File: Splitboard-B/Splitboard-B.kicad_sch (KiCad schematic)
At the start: 109 parts, among them J4 USB_C_Receptacle, K39 KEYSW, K40 KEYSW, K41 KEYSW, K42 KEYSW, K43 KEYSW, K44 KEYSW, K45 KEYSW, K46 KEYSW, K47 KEYSW, K48 KEYSW, K49 KEYSW, K50 KEYSW, K51 KEYSW, K52 KEYSW, K53 KEYSW, K54 KEYSW, K55 KEYSW, K56 KEYSW, K57 KEYSW, K58 KEYSW, K59 KEYSW, K60 KEYSW, K61 KEYSW, K62 KEYSW, K63 KEYSW, K64 KEYSW, K65 KEYSW, K66 KEYSW, K67 KEYSW, K68 KEYSW, K69 KEYSW, K70 KEYSW, K71 KEYSW, K72 KEYSW, K73 KEYSW, K74 KEYSW, K75 KEYSW, K76 KEYSW, U5 CR2013-MI2120

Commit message: updated USB, LCD, ESD, Voltage Reg in schematic
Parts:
- removed C17, C18, C19, C20, C21, C22, C23, C24: 100nF, symbol Device:C
- removed F?: 500mA, Fuse:Fuse_BelFuse_0ZRE0125FF_L21.2mm_W5.3mm, symbol Device:Fuse
- removed R6, R8: 4.7K, symbol Device:R
- added R? (x2): 4K7, symbol Device:R
- added R?: 10k, Resistor_SMD:R_0805_2012Metric, symbol Device:R
- J4: footprint USB_C_Receptacle_GCT_USB4085 -> Connector_USB:USB_C_Receptacle_Amphenol_12401548E4-2A
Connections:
- net +3.3V: now also U5.8 (LED), R?.1, R?.1, R?.2
- net ENC_A: now also U?.1 (GPB0); no longer U?.27 (GPA6)
- net ENC_B: now also U?.2 (GPB1); no longer U?.28 (GPA7)
- net ENC_SW: now also U?.27 (GPA6), R?.1; no longer U?.1 (GPB0)
- net MOSI: now also J4.A5 (CC1), J4.B5 (CC2); no longer J4.B11 (RX1+)
- net SCK: now also J4.A8 (SBU1), J4.B8 (SBU2); no longer J4.A2 (TX1+)
- net SCL: now also J4.A7 (D-), J4.B7 (D-), R?.2; no longer J4.A10 (RX2-)
- net SDA: now also J4.A6 (D+), J4.B6 (D+), R?.2; no longer J4.A11 (RX2+)
- net row0: now also U?.3 (GPB2); no longer U?.2 (GPB1)
- net row1: now also U?.4 (GPB3); no longer U?.3 (GPB2)
- net row2: now also U?.5 (GPB4); no longer U?.4 (GPB3)
- net row3: now also U?.6 (GPB5); no longer U?.5 (GPB4)
- net row4: now also U?.7 (GPB6); no longer U?.6 (GPB5)
- net row5: now also U?.8 (GPB7); no longer U?.7 (GPB6)
- net row6: now also U?.28 (GPA7); no longer U?.8 (GPB7)
- net LCD2_RST: now reaches J4.B3 (TX2-)
- net LCD2_RST: now also J4.A3 (TX1-)
- net LCD2_RESET: now reaches U5.4 (RESET)
- net LCD2_DC: now reaches U5.5 (D/~{C})
- net LCD2_DC: now also J4.A11 (RX2+), J4.B11 (RX1+)
- net at D?.1 (K): now also FB?.1
- net CS renamed LCD2_CS
- net LCD2_CS: now also J4.A10 (RX2-)
- net MISO: no longer names the net of U5.9 (MISO)
- net MISO: no longer J4.A3 (TX1-)
- no-connect marks 6 -> 9
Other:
- note removed: "I2C Pullup"
- moved on the sheet: C15, C16, C?, D?, FB?, U?

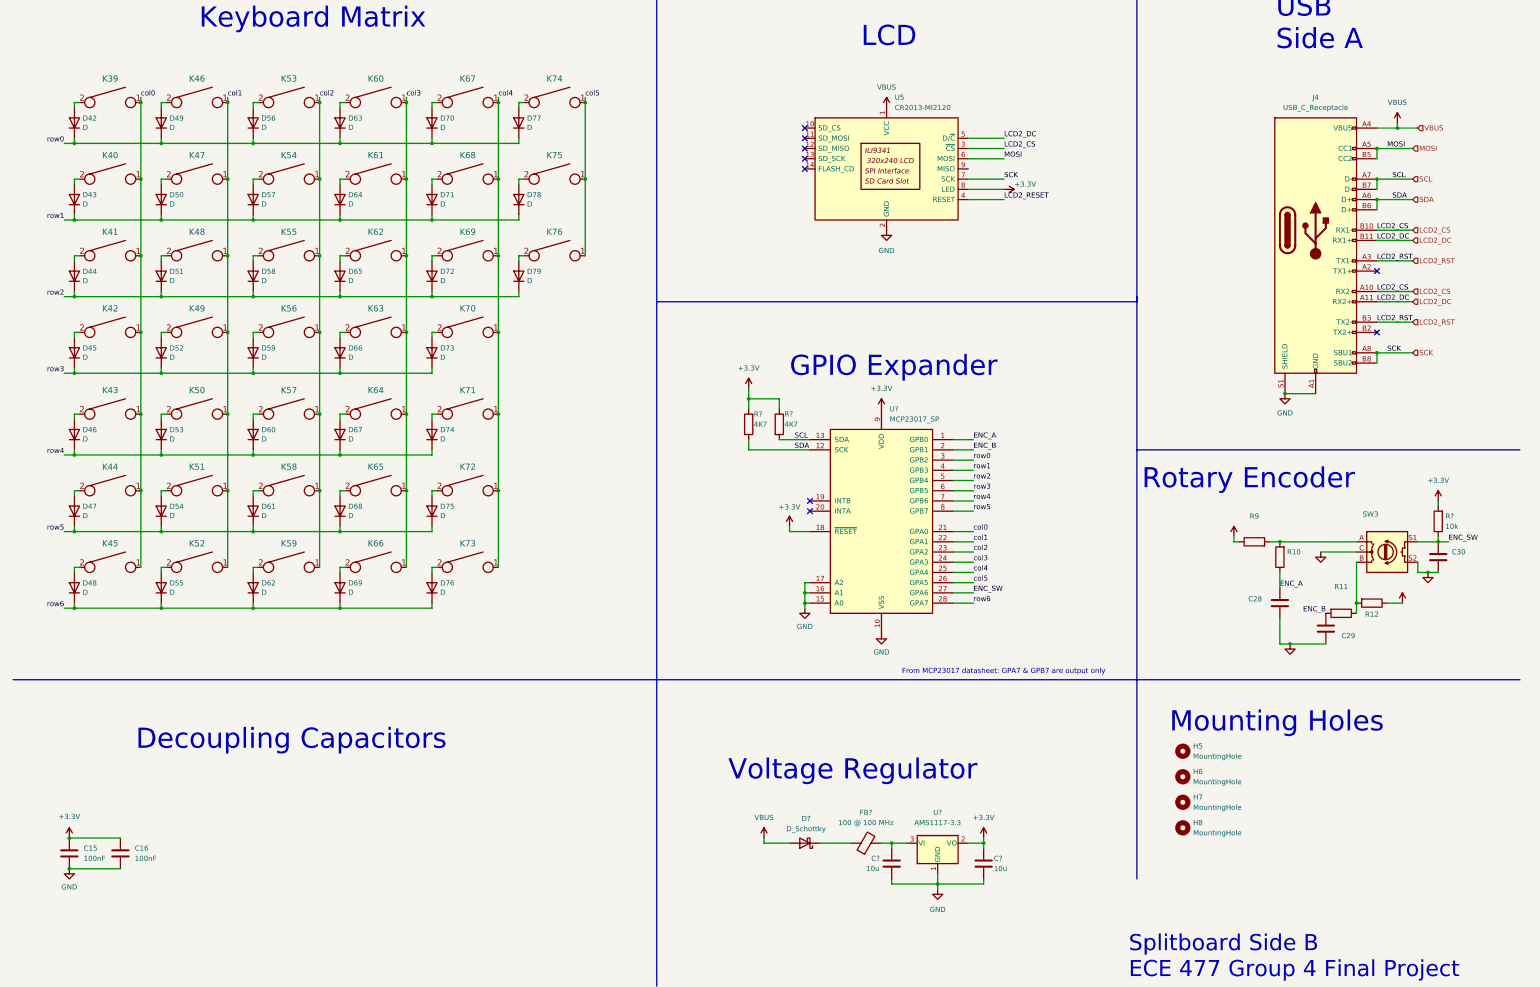
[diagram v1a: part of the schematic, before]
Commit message: assigned new component footprints
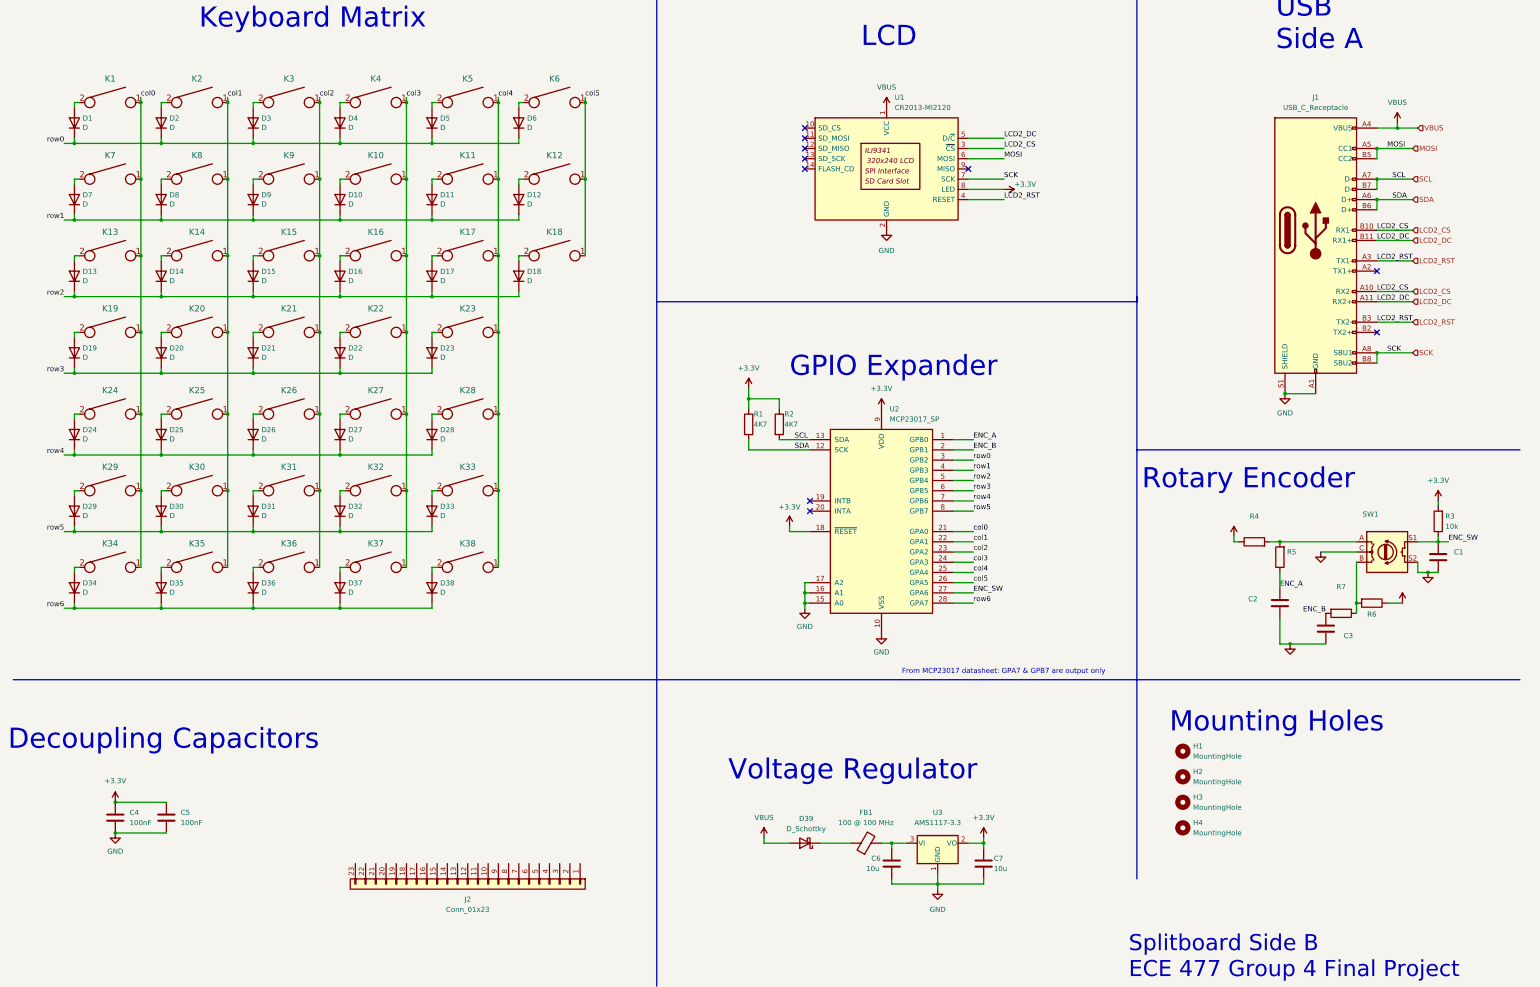
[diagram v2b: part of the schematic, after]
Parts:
- added J2: Conn_01x23, Connector_PinHeader_2.54mm:PinHeader_1x23_P2.54mm_Horizontal, symbol Connector_Generic:Conn_01x23
- gave numbers to parts that had none: 9
- renumbered C30 to C1, C28 to C2, C29 to C3, C15 to C4, C16 to C5, D42 to D1, D64 to D10, D71 to D11, D78 to D12, D44 to D13, D51 to D14, D58 to D15, D65 to D16, D72 to D17, D79 to D18, D45 to D19, D49 to D2, D52 to D20, D59 to D21, D66 to D22, D73 to D23, D46 to D24, D53 to D25, D60 to D26, D67 to D27, D74 to D28, D47 to D29, D56 to D3, D54 to D30, D61 to D31, D68 to D32, D75 to D33, D48 to D34, D55 to D35, D62 to D36, D69 to D37, D76 to D38, D63 to D4, D70 to D5, D77 to D6, D43 to D7, D50 to D8, D57 to D9, H5 to H1, H6 to H2, H7 to H3, H8 to H4, J4 to J1, K39 to K1, K61 to K10, K68 to K11, K75 to K12, K41 to K13, K48 to K14, K55 to K15, K62 to K16, K69 to K17, K76 to K18, K42 to K19, K46 to K2, K49 to K20, K56 to K21, K63 to K22, K70 to K23, K43 to K24, K50 to K25, K57 to K26, K64 to K27, K71 to K28, K44 to K29, K53 to K3, K51 to K30, K58 to K31, K65 to K32, K72 to K33, K45 to K34, K52 to K35, K59 to K36, K66 to K37, K73 to K38, K60 to K4, K67 to K5, K74 to K6, K40 to K7, K47 to K8, K54 to K9, R9 to R4, R10 to R5, R12 to R6, R11 to R7, SW3 to SW1, U5 to U1
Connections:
- net LCD2_RESET is gone; now on net LCD2_RST: U1.4 (RESET)
- no-connect marks 9 -> 10
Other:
- moved on the sheet: C4, C5

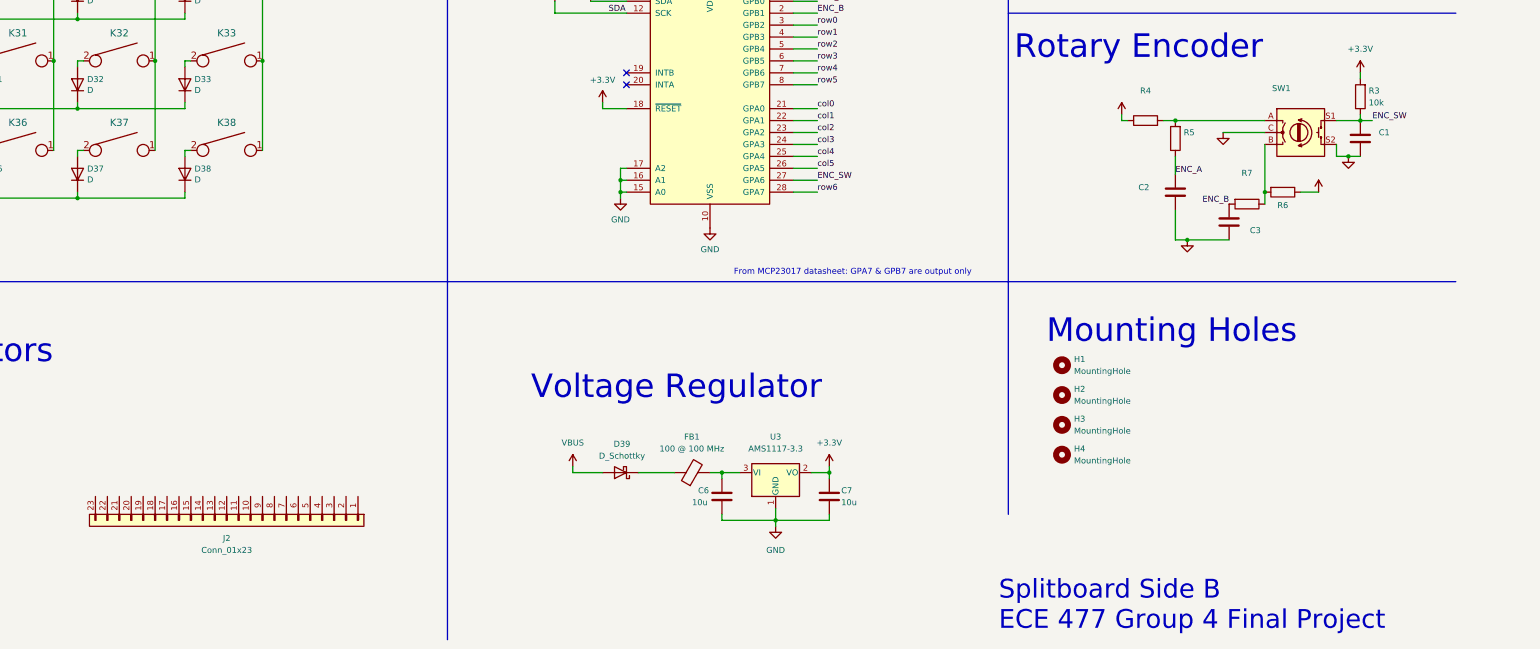
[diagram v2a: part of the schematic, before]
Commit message: Added debugging header to splitboard B
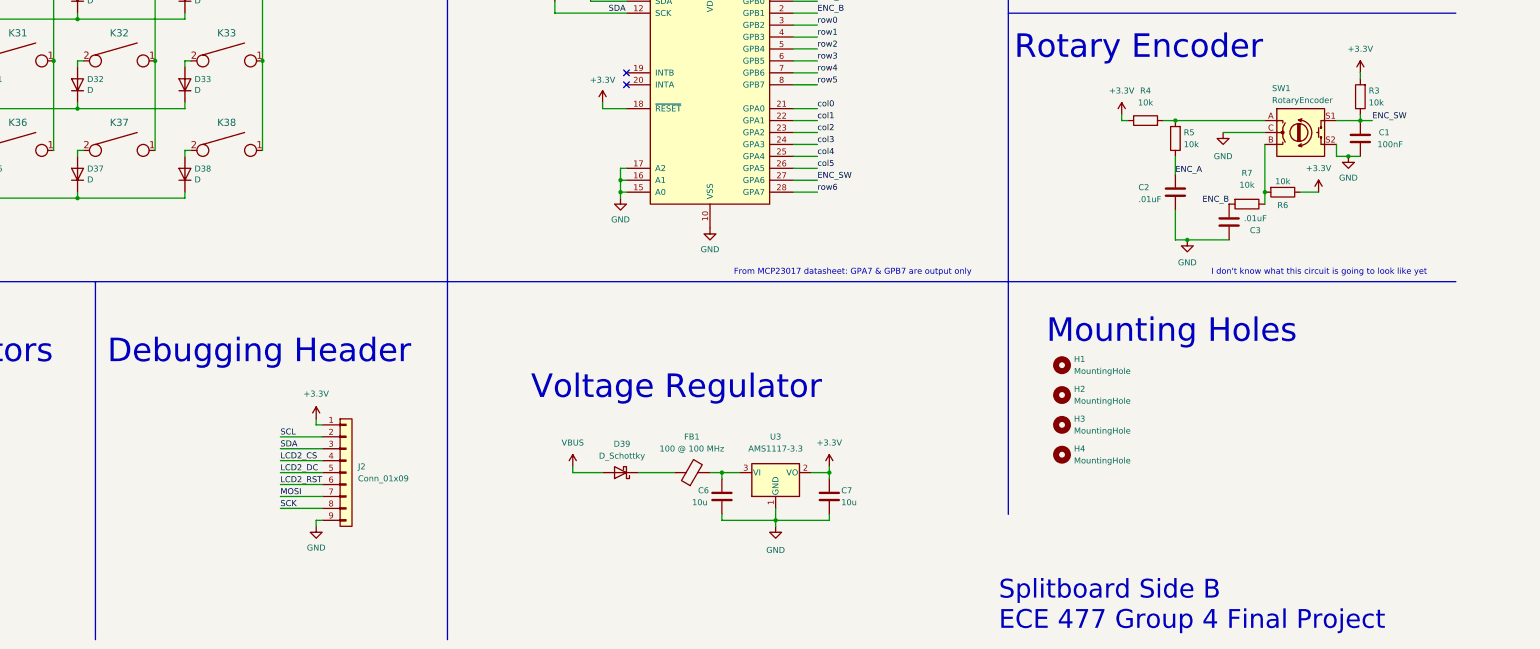
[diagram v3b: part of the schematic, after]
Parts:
- removed J2: Conn_01x23, Connector_PinHeader_2.54mm:PinHeader_1x23_P2.54mm_Horizontal, symbol Connector_Generic:Conn_01x23
- added J2: Conn_01x09, Connector_PinHeader_2.54mm:PinHeader_1x09_P2.54mm_Horizontal, symbol Connector_Generic:Conn_01x09
- C1: value (none) -> 100nF
- C2, C3: value (none) -> .01uF
- R4, R5, R6, R7: value (none) -> 10k
- SW1: value (none) -> RotaryEncoder; footprint (none) -> Rotary_Encoder:RotaryEncoder_Alps_EC12E_Vertical_H20mm
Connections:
- net +3.3V: now also J2.1 (Pin_1)
- net GND: now also J2.9 (Pin_9)
- net LCD2_CS: now also J2.4 (Pin_4)
- net LCD2_DC: now also J2.5 (Pin_5)
- net LCD2_RST: now also J2.6 (Pin_6)
- net MOSI: now also J2.7 (Pin_7)
- net SCK: now also J2.8 (Pin_8)
- net SCL: now also J2.2 (Pin_2)
- net SDA: now also J2.3 (Pin_3)
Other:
- note added: "Debugging Header"
- note added: "I don't know what this circuit is going to look like yet"

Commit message: Splitboard B schematic completed, added some additional notes on board A
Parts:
- SW1: footprint Rotary_Encoder:RotaryEncoder_Alps_EC12E_Vertical_H20mm -> Rotary_Encoder:RotaryEncoder_Alps_EC11E-Switch_Vertical_H20mm
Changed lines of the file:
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@@
       (effects (font (size 1.27 1.27)) (justify left))
     )
-    (property "Footprint" "Rotary_Encoder:RotaryEncoder_Alps_EC12E_Vertical_H20mm" (id 2) (at 363.22 157.226 0)
+    (property "Footprint" "Rotary_Encoder:RotaryEncoder_Alps_EC11E-Switch_Vertical_H20mm" (id 2) (at 363.22 157.226 0)
       (effects (font (size 1.27 1.27)) hide)
     )
@@
     )
     (path "/92527856-d3ca-4bc5-b4fe-d85867977214"
-      (reference "SW1") (unit 1) (value "RotaryEncoder") (footprint "Rotary_Encoder:RotaryEncoder_Alps_EC12E_Vertical_H20mm")
+      (reference "SW1") (unit 1) (value "RotaryEncoder") (footprint "Rotary_Encoder:RotaryEncoder_Alps_EC11E-Switch_Vertical_H20mm")
     )
     (path "/3a31ae65-de49-4f48-8038-a331a3ecf694"

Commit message: Routing PCB
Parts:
- C1, C2, C3, C4, C5: footprint (none) -> Capacitor_SMD:C_0805_2012Metric
- R1, R2, R4, R5, R6, R7: footprint (none) -> Resistor_SMD:R_0805_2012Metric
- renumbered D14 to D10, D20 to D11, D25 to D12, D30 to D13, D35 to D14, D3 to D15, D9 to D16, D15 to D17, D21 to D18, D26 to D19, D7 to D2, D31 to D20, D36 to D21, D4 to D22, D10 to D23, D16 to D24, D22 to D25, D27 to D26, D32 to D27, D37 to D28, D5 to D29, D13 to D3, D11 to D30, D17 to D31, D23 to D32, D28 to D33, D33 to D34, D38 to D35, D6 to D36, D12 to D37, D18 to D38, D19 to D4, D24 to D5, D29 to D6, D34 to D7, D2 to D8, D8 to D9, K14 to K10, K20 to K11, K25 to K12, K30 to K13, K35 to K14, K3 to K15, K9 to K16, K15 to K17, K21 to K18, K26 to K19, K7 to K2, K31 to K20, K36 to K21, K4 to K22, K10 to K23, K16 to K24, K22 to K25, K27 to K26, K32 to K27, K37 to K28, K5 to K29, K13 to K3, K11 to K30, K17 to K31, K23 to K32, K28 to K33, K33 to K34, K38 to K35, K6 to K36, K12 to K37, K18 to K38, K19 to K4, K24 to K5, K29 to K6, K34 to K7, K2 to K8, K8 to K9
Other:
- moved on the sheet: D1, D10, D11, D12, D13, D14, D15, D16, D17, D18, D19, D2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

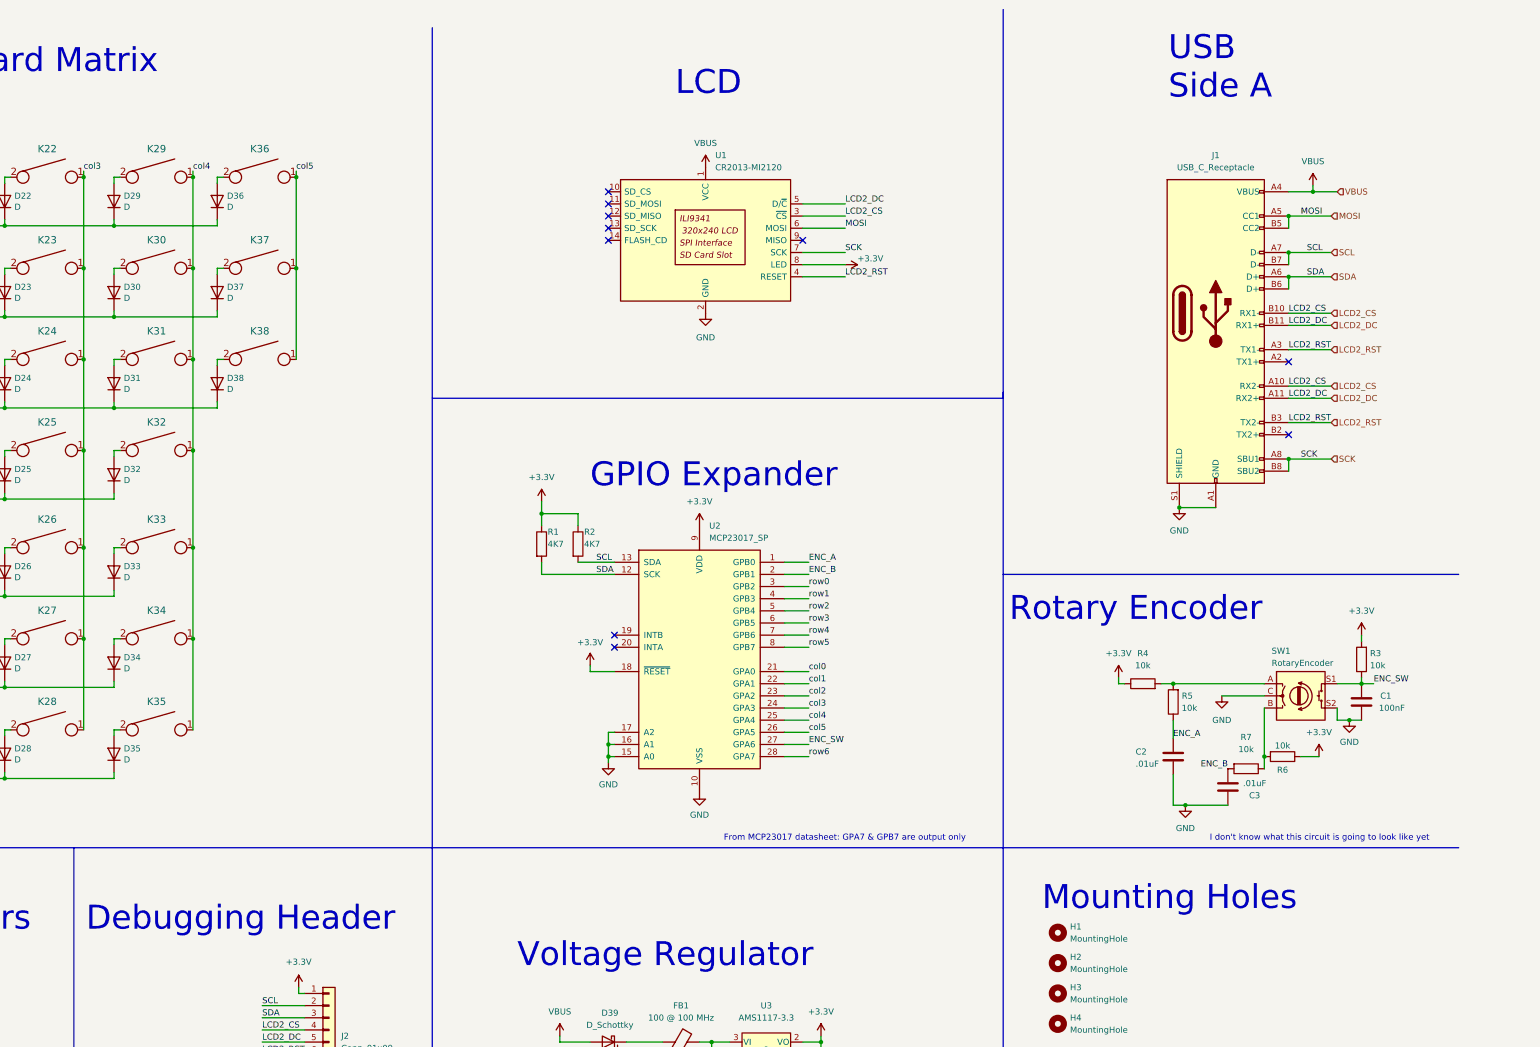
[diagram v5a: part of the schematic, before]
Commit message: added more archive files
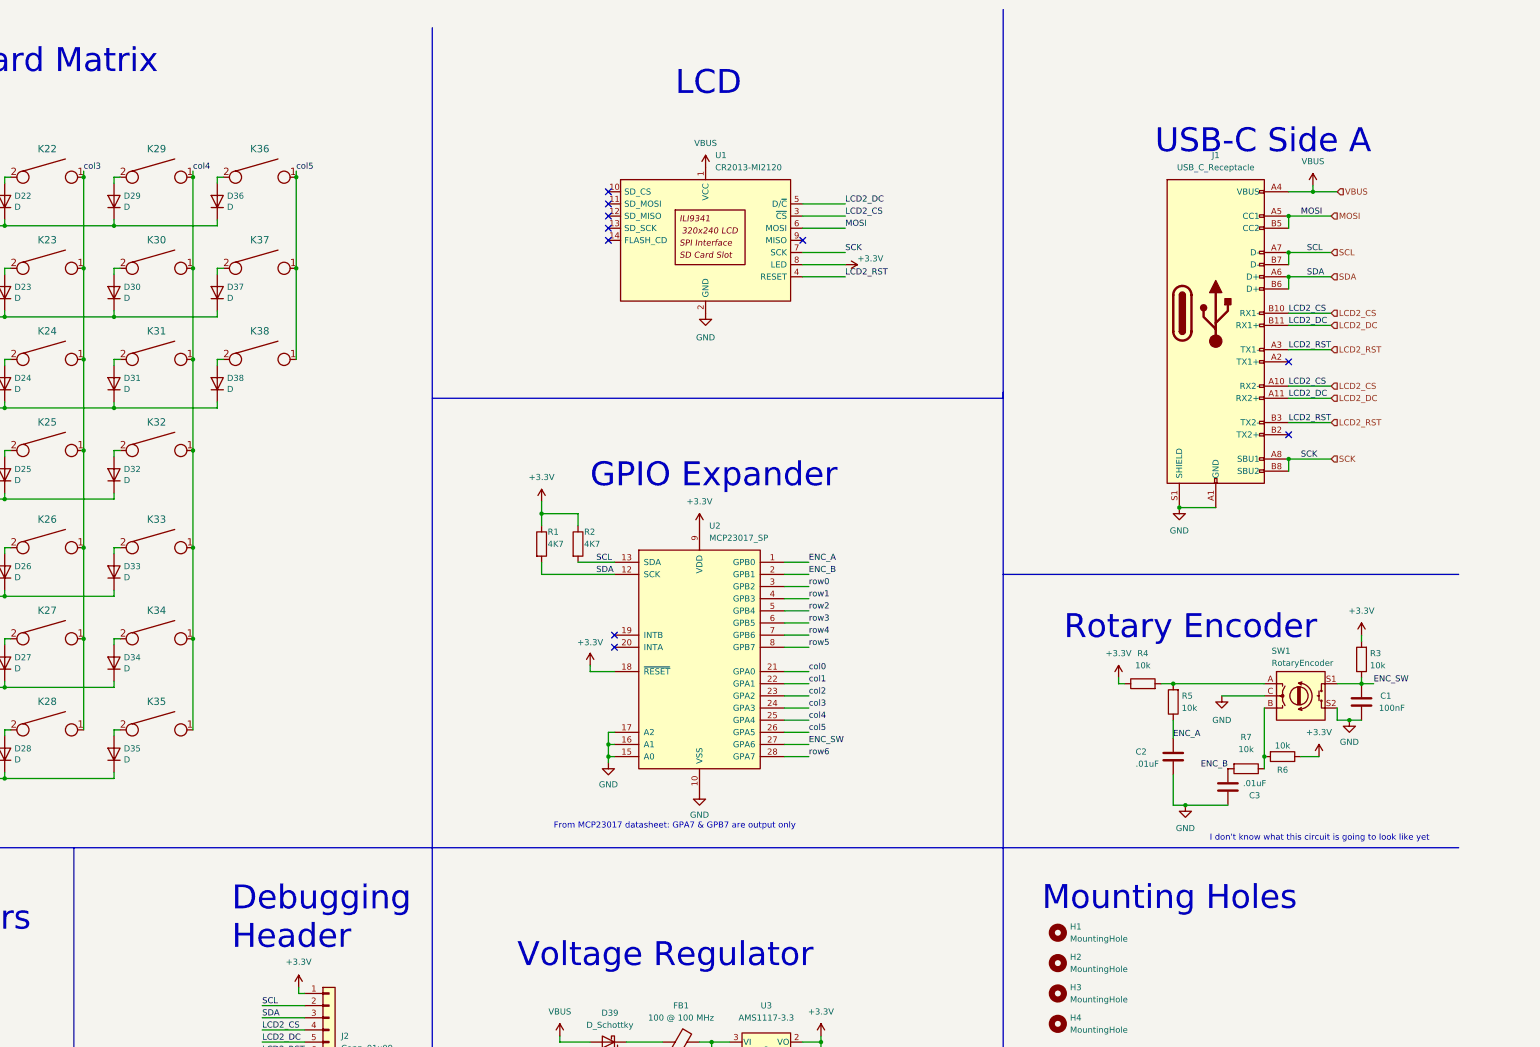
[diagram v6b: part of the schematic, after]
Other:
- note added: "USB-C Side A"
- note removed: "USB Side A"
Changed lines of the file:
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@@
   )
   (text "From MCP23017 datasheet: GPA7 & GPB7 are output only"
-    (at 246.38 191.77 0)
+    (at 210.82 189.23 0)
     (effects (font (size 1.27 1.27)) (justify left bottom))
   )
-  (text "Debugging Header" (at 113.03 210.82 0)
+  (text "Debugging\nHeader" (at 143.51 214.63 0)
     (effects (font (size 5 5)) (justify left bottom))
   )
@@
     (effects (font (size 5 5)) (justify left bottom))
   )
-  (text "USB\nSide A" (at 339.344 36.83 0)
+  (text "USB-C Side A" (at 336.55 48.26 0)
     (effects (font (size 5 5)) (justify left bottom))
   )
@@
     (effects (font (size 5 5)) (justify left bottom))
   )
-  (text "Rotary Encoder" (at 306.07 146.05 0)
+  (text "Rotary Encoder" (at 317.5 149.86 0)
     (effects (font (size 5 5)) (justify left bottom))
   )
